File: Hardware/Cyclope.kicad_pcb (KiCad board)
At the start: 2 copper layers, 100 x 84 mm, 81 parts, among them J1 M20-9762042, J2 Motor_2, J3 Motor_1, J4 Front, J5 Front, J8 FTDI, M1 FS5113R, M2 FS5113R, Q1 DMG3414U, Q2 DMG2301L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

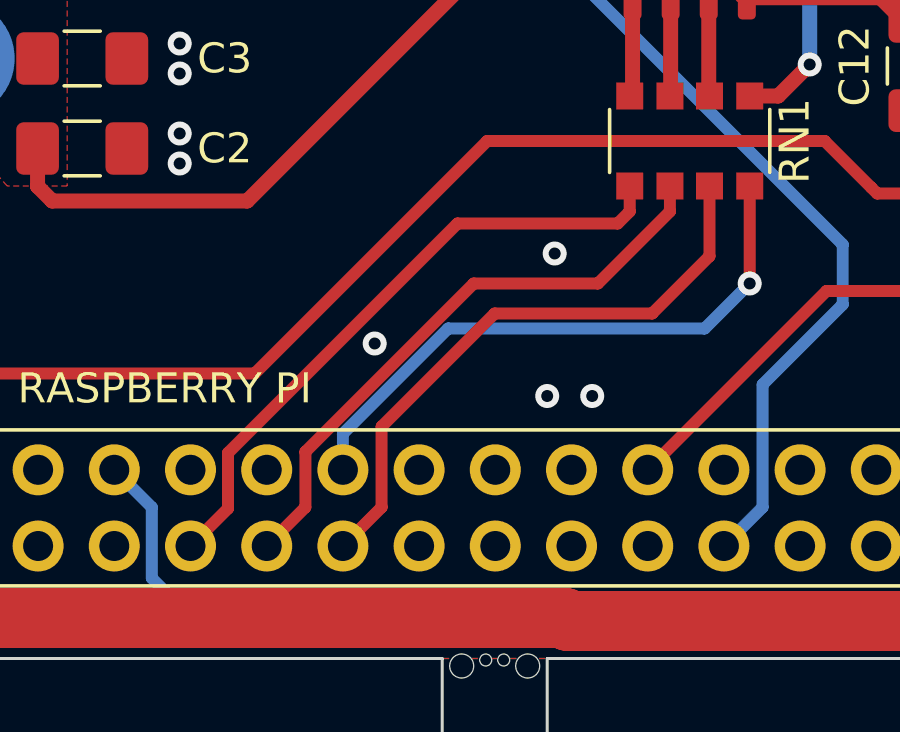
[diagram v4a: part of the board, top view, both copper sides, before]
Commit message: [Hardware] Used slightly narrower tracks for ADC SPI bus to have more clearance between 40-pin connector pins.
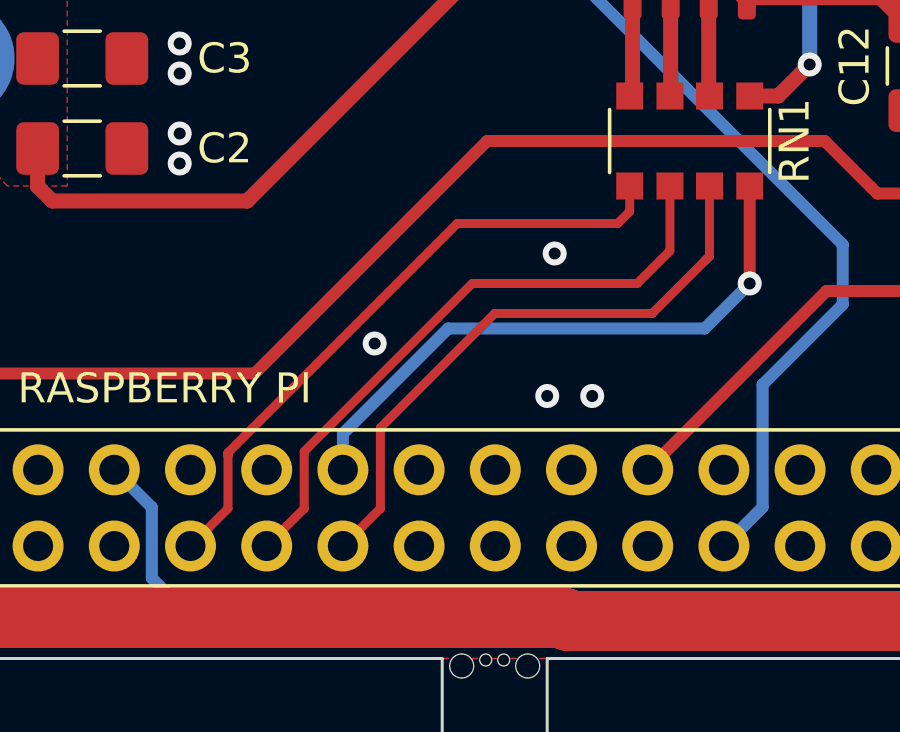
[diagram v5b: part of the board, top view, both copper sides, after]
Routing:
- net ADC_SPI_MISO: track 20.0 -> 20.8 mm
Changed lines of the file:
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@@
     (thickness 1.6)
     (drawings 66)
-    (tracks 376)
+    (tracks 378)
     (zones 0)
     (modules 81)
@@
   )
   (setup
-    (last_trace_width 0.4)
+    (last_trace_width 0.3)
+    (user_trace_width 0.3)
     (user_trace_width 0.4)
     (user_trace_width 0.5)
@@
   (segment (start 114.635 79.6025) (end 114.7375 79.5) (width 0.5) (layer F.Cu) (net 32))
   (segment (start 114.635 82.775) (end 114.635 79.6025) (width 0.5) (layer F.Cu) (net 32))
-  (segment (start 101.189999 104.960001) (end 99.9 106.25) (width 0.4) (layer F.Cu) (net 33))
-  (segment (start 101.189999 103.109999) (end 101.189999 104.960001) (width 0.4) (layer F.Cu) (net 33))
-  (segment (start 106.799998 97.5) (end 101.189999 103.109999) (width 0.4) (layer F.Cu) (net 33))
-  (segment (start 110.94 97.5) (end 106.799998 97.5) (width 0.4) (layer F.Cu) (net 33))
-  (segment (start 113.34 95.1) (end 110.94 97.5) (width 0.4) (layer F.Cu) (net 33))
-  (segment (start 113.34 94.25) (end 113.34 95.1) (width 0.4) (layer F.Cu) (net 33))
-  (segment (start 112 95.1) (end 112 94.25) (width 0.4) (layer F.Cu) (net 34))
-  (segment (start 111.6 95.5) (end 112 95.1) (width 0.4) (layer F.Cu) (net 34))
-  (segment (start 106.259998 95.5) (end 111.6 95.5) (width 0.4) (layer F.Cu) (net 34))
-  (segment (start 98.610001 103.149997) (end 106.259998 95.5) (width 0.4) (layer F.Cu) (net 34))
-  (segment (start 98.610001 104.999999) (end 98.610001 103.149997) (width 0.4) (layer F.Cu) (net 34))
-  (segment (start 97.36 106.25) (end 98.610001 104.999999) (width 0.4) (layer F.Cu) (net 34))
+  (segment (start 112.25 97.5) (end 113.34 96.41) (width 0.3) (layer F.Cu) (net 33))
+  (segment (start 101.150001 103.099999) (end 106.75 97.5) (width 0.3) (layer F.Cu) (net 33))
+  (segment (start 113.34 96.41) (end 113.34 94.25) (width 0.3) (layer F.Cu) (net 33))
+  (segment (start 106.75 97.5) (end 112.25 97.5) (width 0.3) (layer F.Cu) (net 33))
+  (segment (start 101.150001 104.999999) (end 101.150001 103.099999) (width 0.3) (layer F.Cu) (net 33))
+  (segment (start 99.9 106.25) (end 101.150001 104.999999) (width 0.3) (layer F.Cu) (net 33))
+  (segment (start 98.610001 103.139999) (end 98.610001 103.25) (width 0.3) (layer F.Cu) (net 34))
+  (segment (start 98.610001 104.999999) (end 97.36 106.25) (width 0.3) (layer F.Cu) (net 34))
+  (segment (start 98.610001 103.139999) (end 98.610001 104.999999) (width 0.3) (layer F.Cu) (net 34))
+  (segment (start 111.6 95.5) (end 112 95.1) (width 0.3) (layer F.Cu) (net 34))
+  (segment (start 112 95.1) (end 112 94.25) (width 0.3) (layer F.Cu) (net 34))
+  (segment (start 106.25 95.5) (end 111.6 95.5) (width 0.3) (layer F.Cu) (net 34))
+  (segment (start 98.610001 103.139999) (end 106.25 95.5) (width 0.3) (layer F.Cu) (net 34))
   (segment (start 102.44 102.507919) (end 105.947919 99) (width 0.4) (layer B.Cu) (net 35))
   (segment (start 102.44 103.71) (end 102.44 102.507919) (width 0.4) (layer B.Cu) (net 35))
@@
   (via (at 116 97.5) (size 0.8) (drill 0.4) (layers F.Cu B.Cu) (net 35))
   (segment (start 116 94.25) (end 116 97.5) (width 0.4) (layer F.Cu) (net 35))
-  (segment (start 103.729999 104.960001) (end 102.44 106.25) (width 0.4) (layer F.Cu) (net 36))
-  (segment (start 103.729999 102.270001) (end 103.729999 104.960001) (width 0.4) (layer F.Cu) (net 36))
-  (segment (start 107.5 98.5) (end 103.729999 102.270001) (width 0.4) (layer F.Cu) (net 36))
-  (segment (start 112.75 98.5) (end 107.5 98.5) (width 0.4) (layer F.Cu) (net 36))
-  (segment (start 114.66 96.59) (end 112.75 98.5) (width 0.4) (layer F.Cu) (net 36))
-  (segment (start 114.66 94.25) (end 114.66 96.59) (width 0.4) (layer F.Cu) (net 36))
+  (segment (start 114.66 96.59) (end 114.5 96.75) (width 0.3) (layer F.Cu) (net 36))
+  (segment (start 114.66 94.25) (end 114.66 96.59) (width 0.3) (layer F.Cu) (net 36))
+  (segment (start 114.66 96.59) (end 112.75 98.5) (width 0.3) (layer F.Cu) (net 36))
+  (segment (start 107.5 98.5) (end 112.75 98.5) (width 0.3) (layer F.Cu) (net 36))
+  (segment (start 103.690001 102.309999) (end 107.5 98.5) (width 0.3) (layer F.Cu) (net 36))
+  (segment (start 103.690001 104.999999) (end 103.690001 102.309999) (width 0.3) (layer F.Cu) (net 36))
+  (segment (start 102.44 106.25) (end 103.690001 104.999999) (width 0.3) (layer F.Cu) (net 36))
   (segment (start 113.365 91.225) (end 113.34 91.25) (width 0.5) (layer F.Cu) (net 37))
   (segment (start 113.365 87.725) (end 113.365 91.225) (width 0.5) (layer F.Cu) (net 37))

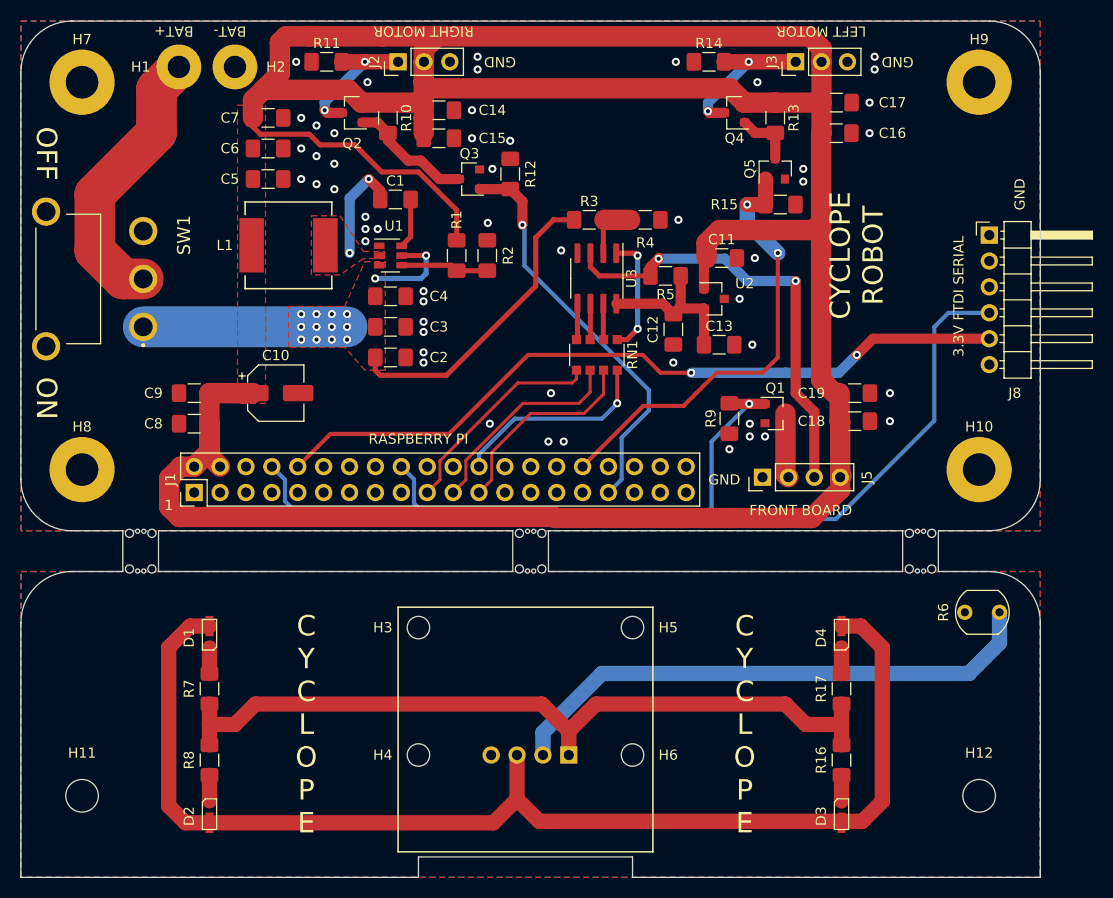
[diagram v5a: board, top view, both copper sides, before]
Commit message: [Hardware] Improved motherboard PCB to use a 0.25mm trace clearance.
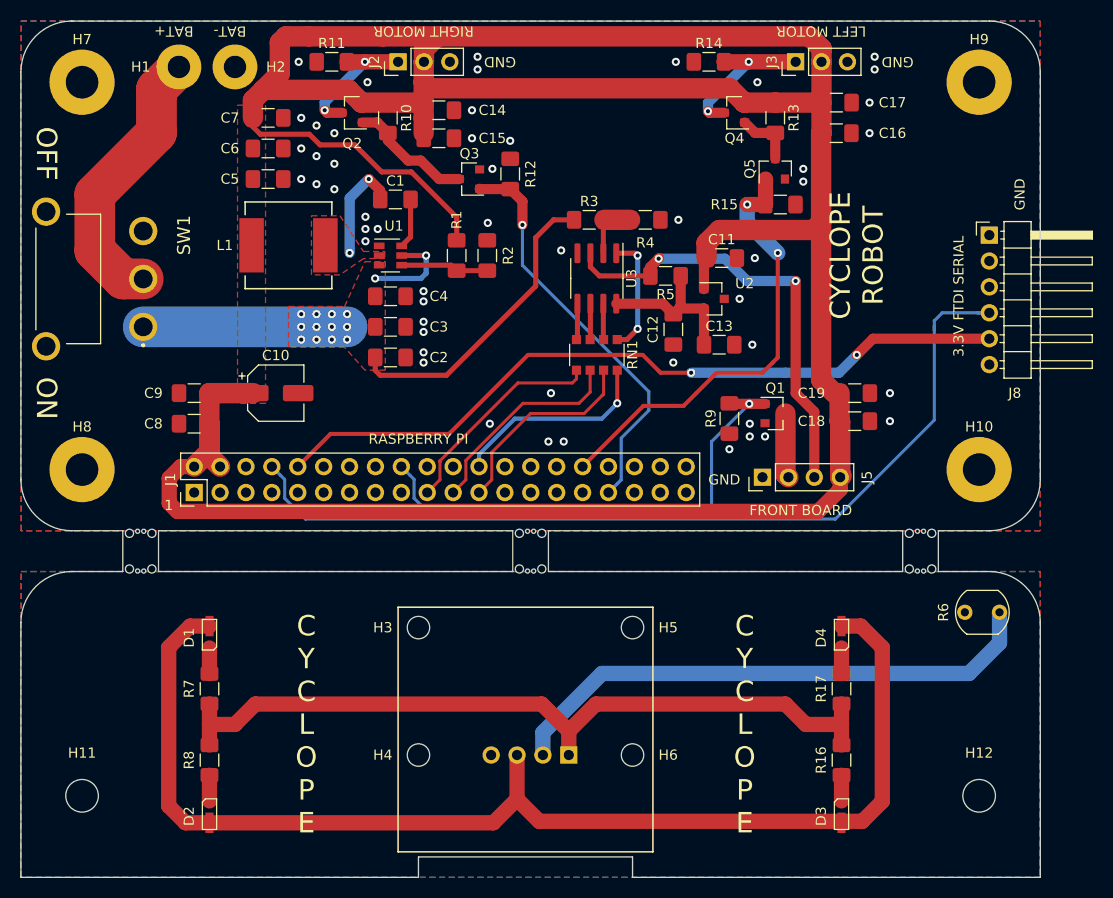
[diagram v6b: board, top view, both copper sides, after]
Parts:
- moved R11 0.50 mm to (88.0, 64.0)
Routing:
- net /Raspberry_Pi/UART_TX: track 87.5 -> 89.3 mm
- net +5V: track 314.6 -> 313.4 mm
- net Net-(J2-Pad1): track 13.7 -> 13.2 mm

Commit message: [Hardware] Removed mechanical supply parts unrelated with PCB, added battery holder supply part.
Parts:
- removed M1, M2: FS5113R, Supply_Part:Supply_Part
- removed MP1, MP2: FS5103R-W, Supply_Part:Supply_Part
- removed MP3, MP4: ASB01, Supply_Part:Supply_Part
- added BAT1: MP000303, Supply_Part:Supply_Part, F.Cu at (33.8, 162.8)
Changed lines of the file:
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@@
     (tracks 383)
     (zones 0)
-    (modules 81)
+    (modules 76)
     (nets 62)
   )
@@
   )
   (setup
-    (last_trace_width 1.5)
+    (last_trace_width 0.25)
     (user_trace_width 0.3)
     (user_trace_width 0.4)
@@
     (add_net "Net-(SW1-Pad3)")
   )
+  (module Supply_Part:Supply_Part (layer F.Cu)
+    (at 33.75 162.75)
+    (attr virtual)
+    (fp_text reference BAT1 (at -3.175 3.81) (layer Eco1.User)
+      (effects (font (size 1 1) (thickness 0.15)))
+    )
+    (fp_text value MP000303 (at 0 -0.5) (layer F.Fab) hide
+      (effects (font (size 1 1) (thickness 0.15)))
+    )
+    (fp_line (start -5.08 2.54) (end -5.08 0) (layer Eco1.User) (width 0.12))
+    (fp_line (start 5.08 2.54) (end -5.08 2.54) (layer Eco1.User) (width 0.12))
+    (fp_line (start 5.08 -2.54) (end 5.08 2.54) (layer Eco1.User) (width 0.12))
+    (fp_line (start -5.08 -2.54) (end 5.08 -2.54) (layer Eco1.User) (width 0.12))
+    (fp_line (start -5.08 0) (end -5.08 -2.54) (layer Eco1.User) (width 0.12))
+  )
   (module Capacitor_SMD:C_1206_3216Metric_Pad1.42x1.75mm_HandSolder (layer F.Cu)
     (at 81.75 69.5 180)
@@
     )
   )
-  (module Supply_Part:Supply_Part (layer F.Cu)
-    (at 35.804001 189.73)
-    (attr virtual)
-    (fp_text reference MP4 (at -3.175 3.81) (layer Eco1.User)
-      (effects (font (size 1 1) (thickness 0.15)))
-    )
-    (fp_text value ASB01 (at 0 -0.5) (layer F.Fab) hide
-      (effects (font (size 1 1) (thickness 0.15)))
-    )
-    (fp_line (start -5.08 2.54) (end -5.08 0) (layer Eco1.User) (width 0.12))
-    (fp_line (start 5.08 2.54) (end -5.08 2.54) (layer Eco1.User) (width 0.12))
-    (fp_line (start 5.08 -2.54) (end 5.08 2.54) (layer Eco1.User) (width 0.12))
-    (fp_line (start -5.08 -2.54) (end 5.08 -2.54) (layer Eco1.User) (width 0.12))
-    (fp_line (start -5.08 0) (end -5.08 -2.54) (layer Eco1.User) (width 0.12))
-  )
-  (module Supply_Part:Supply_Part (layer F.Cu)
-    (at 35.804001 183.53)
-    (attr virtual)
-    (fp_text reference MP3 (at -3.175 3.81) (layer Eco1.User)
-      (effects (font (size 1 1) (thickness 0.15)))
-    )
-    (fp_text value ASB01 (at 0 -0.5) (layer F.Fab) hide
-      (effects (font (size 1 1) (thickness 0.15)))
-    )
-    (fp_line (start -5.08 2.54) (end -5.08 0) (layer Eco1.User) (width 0.12))
-    (fp_line (start 5.08 2.54) (end -5.08 2.54) (layer Eco1.User) (width 0.12))
-    (fp_line (start 5.08 -2.54) (end 5.08 2.54) (layer Eco1.User) (width 0.12))
-    (fp_line (start -5.08 -2.54) (end 5.08 -2.54) (layer Eco1.User) (width 0.12))
-    (fp_line (start -5.08 0) (end -5.08 -2.54) (layer Eco1.User) (width 0.12))
-  )
-  (module Supply_Part:Supply_Part (layer F.Cu)
-    (at 24.524001 189.73)
-    (attr virtual)
-    (fp_text reference MP2 (at -3.175 3.81) (layer Eco1.User)
-      (effects (font (size 1 1) (thickness 0.15)))
-    )
-    (fp_text value FS5103R-W (at 0 -0.5) (layer F.Fab) hide
-      (effects (font (size 1 1) (thickness 0.15)))
-    )
-    (fp_line (start -5.08 2.54) (end -5.08 0) (layer Eco1.User) (width 0.12))
-    (fp_line (start 5.08 2.54) (end -5.08 2.54) (layer Eco1.User) (width 0.12))
-    (fp_line (start 5.08 -2.54) (end 5.08 2.54) (layer Eco1.User) (width 0.12))
-    (fp_line (start -5.08 -2.54) (end 5.08 -2.54) (layer Eco1.User) (width 0.12))
-    (fp_line (start -5.08 0) (end -5.08 -2.54) (layer Eco1.User) (width 0.12))
-  )
-  (module Supply_Part:Supply_Part (layer F.Cu)
-    (at 35.804001 177.33)
-    (attr virtual)
-    (fp_text reference MP1 (at -3.175 3.81) (layer Eco1.User)
-      (effects (font (size 1 1) (thickness 0.15)))
-    )
-    (fp_text value FS5103R-W (at 0 -0.5) (layer F.Fab) hide
-      (effects (font (size 1 1) (thickness 0.15)))
-    )
-    (fp_line (start -5.08 2.54) (end -5.08 0) (layer Eco1.User) (width 0.12))
-    (fp_line (start 5.08 2.54) (end -5.08 2.54) (layer Eco1.User) (width 0.12))
-    (fp_line (start 5.08 -2.54) (end 5.08 2.54) (layer Eco1.User) (width 0.12))
-    (fp_line (start -5.08 -2.54) (end 5.08 -2.54) (layer Eco1.User) (width 0.12))
-    (fp_line (start -5.08 0) (end -5.08 -2.54) (layer Eco1.User) (width 0.12))
-  )
-  (module Supply_Part:Supply_Part (layer F.Cu)
-    (at 24.524001 183.53)
-    (attr virtual)
-    (fp_text reference M2 (at -3.175 3.81) (layer Eco1.User)
-      (effects (font (size 1 1) (thickness 0.15)))
-    )
-    (fp_text value FS5113R (at 0 -0.5) (layer F.Fab) hide
-      (effects (font (size 1 1) (thickness 0.15)))
-    )
-    (fp_line (start -5.08 2.54) (end -5.08 0) (layer Eco1.User) (width 0.12))
-    (fp_line (start 5.08 2.54) (end -5.08 2.54) (layer Eco1.User) (width 0.12))
-    (fp_line (start 5.08 -2.54) (end 5.08 2.54) (layer Eco1.User) (width 0.12))
-    (fp_line (start -5.08 -2.54) (end 5.08 -2.54) (layer Eco1.User) (width 0.12))
-    (fp_line (start -5.08 0) (end -5.08 -2.54) (layer Eco1.User) (width 0.12))
-  )
-  (module Supply_Part:Supply_Part (layer F.Cu)
-    (at 24.524001 177.33)
-    (attr virtual)
-    (fp_text reference M1 (at -3.175 3.81) (layer Eco1.User)
-      (effects (font (size 1 1) (thickness 0.15)))
-    )
-    (fp_text value FS5113R (at 0 -0.5) (layer F.Fab) hide
-      (effects (font (size 1 1) (thickness 0.15)))
-    )
-    (fp_line (start -5.08 2.54) (end -5.08 0) (layer Eco1.User) (width 0.12))
-    (fp_line (start 5.08 2.54) (end -5.08 2.54) (layer Eco1.User) (width 0.12))
-    (fp_line (start 5.08 -2.54) (end 5.08 2.54) (layer Eco1.User) (width 0.12))
-    (fp_line (start -5.08 -2.54) (end 5.08 -2.54) (layer Eco1.User) (width 0.12))
-    (fp_line (start -5.08 0) (end -5.08 -2.54) (layer Eco1.User) (width 0.12))
-  )
   (module 158301250:158301250 (layer F.Cu)
     (at 76 137.5 270)
@@
     (effects (font (size 1 1) (thickness 0.15)))
   )
-  (via (at 86.5 70.25) (size 0.8) (drill 0.4) (layers F.Cu B.Cu) (net 3))
-  (via (at 88.25 71) (size 0.8) (drill 0.4) (layers F.Cu B.Cu) (net 3))
   (segment (start 95.725 81.175) (end 94.85 82.05) (width 0.5) (layer F.Cu) (net 1))
   (segment (start 95.725 77.5) (end 95.725 81.175) (width 0.5) (layer F.Cu) (net 1))
@@
   (segment (start 89.75 77.375) (end 91.625 75.5) (width 1) (layer B.Cu) (net 2))
   (segment (start 89.75 82.75) (end 89.75 77.375) (width 1) (layer B.Cu) (net 2))
+  (via (at 86.5 70.25) (size 0.8) (drill 0.4) (layers F.Cu B.Cu) (net 3))
+  (via (at 88.25 71) (size 0.8) (drill 0.4) (layers F.Cu B.Cu) (net 3))
   (via (at 91.3 81.6) (size 0.8) (drill 0.4) (layers F.Cu B.Cu) (net 3))
   (via (at 91.3 80.4) (size 0.8) (drill 0.4) (layers F.Cu B.Cu) (net 3))

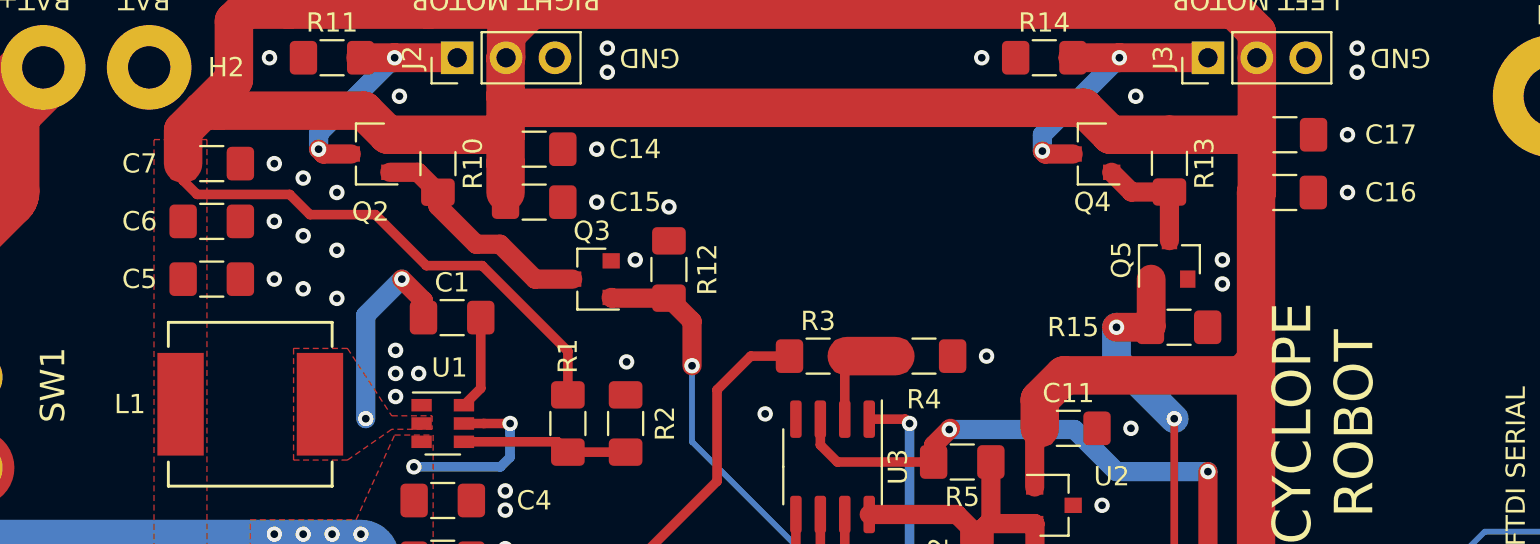
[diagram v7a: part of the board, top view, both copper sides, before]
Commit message: [Hardware] Changed 22u capacitors footprint from 1206 to 1210 as more references are available in 1210 package.
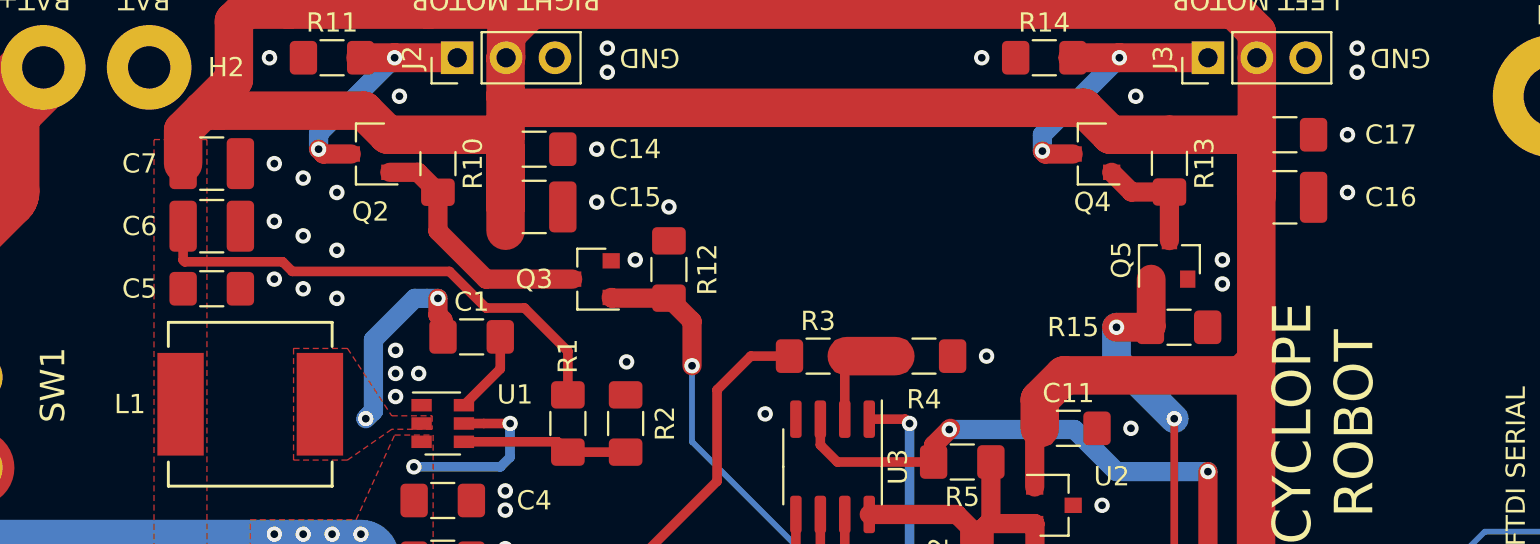
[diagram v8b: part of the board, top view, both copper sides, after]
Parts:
- C15, C16, C6, C7: footprint Capacitor_SMD:C_1206_3216Metric_Pad1.42x1.75mm_HandSolder -> Capacitor_SMD:C_1210_3225Metric_Pad1.42x2.65mm_HandSolder
- moved C1 1.42 mm to (95.2, 78.5)
- moved C5 0.50 mm to (81.8, 76.0)
- moved C16 0.25 mm to (137.5, 71.2)
- moved C15 0.25 mm to (98.5, 71.8)
- moved C6 0.25 mm to (81.8, 72.8)
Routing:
- net +5V: track 313.4 -> 323.7 mm
- net Net-(Q2-Pad1): track 12.2 -> 13.0 mm
- net Net-(C1-Pad2): track 4.91 -> 4.33 mm
